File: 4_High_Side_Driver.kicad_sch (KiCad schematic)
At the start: 32 parts, among them U4 VND7050AJTR, U8 VND7050AJTR

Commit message: All the diodes, and other layout work
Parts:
- D10, D11, D12, D13, D14, D15, D16, D17, D18, D19, D20, D7, D8, D9: footprint Package_TO_SOT_SMD:SOT-23 -> Package_TO_SOT_SMD:SOT-523; LCSC C47546 -> C134414; MPN BAT54S,215 -> BAT54ST-7-F; Manufacturer Nexperia -> Diodes Incorporated
- D6: footprint Diode_SMD:D_0805_2012Metric -> Diode_SMD:D_SOD-123; LCSC (none) -> C83152; MPN (none) -> BAT46W-7-F; Manufacturer (none) -> Diodes Incorporated

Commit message: Layout, smaller resistors and HB + Error LEDs
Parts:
- D10, D11, D12, D13, D14, D17, D18, D19, D20: now in the parts list
- D6: footprint Diode_SMD:D_SOD-123 -> Diode_SMD:D_SOD-523; LCSC C83152 -> C139439; MPN BAT46W-7-F -> SDM20U40-7
- R14, R21: footprint Resistor_SMD:R_0603_1608Metric -> Resistor_SMD:R_0402_1005Metric; now in the parts list
- R15, R16, R22, R23: footprint Resistor_SMD:R_0603_1608Metric -> Resistor_SMD:R_0402_1005Metric; LCSC (none) -> C25756
- R17, R18, R19, R20, R24, R25, R26, R27: footprint Resistor_SMD:R_0603_1608Metric -> Resistor_SMD:R_0402_1005Metric; LCSC (none) -> C25756; now in the parts list
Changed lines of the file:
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@@
 		(unit 1)
 		(exclude_from_sim no)
-		(in_bom no)
-		(on_board no)
+		(in_bom yes)
+		(on_board yes)
 		(dnp no)
 		(fields_autoplaced yes)
@@
 		(unit 1)
 		(exclude_from_sim no)
-		(in_bom no)
-		(on_board no)
+		(in_bom yes)
+		(on_board yes)
 		(dnp no)
 		(property "Reference" "R26"
@@
 			)
 		)
-		(property "Footprint" "Resistor_SMD:R_0603_1608Metric"
+		(property "Footprint" "Resistor_SMD:R_0402_1005Metric"
 			(at 139.7 102.362 90)
 			(effects
@@
 			)
 		)
-		(property "LCSC" ""
+		(property "LCSC" "C25756"
 			(at 139.7 104.14 0)
 			(effects
@@
 		(unit 1)
 		(exclude_from_sim no)
-		(in_bom no)
-		(on_board no)
+		(in_bom yes)
+		(on_board yes)
 		(dnp no)
 		(fields_autoplaced yes)
@@
 		(unit 1)
 		(exclude_from_sim no)
-		(in_bom no)
-		(on_board no)
+		(in_bom yes)
+		(on_board yes)
 		(dnp no)
 		(property "Reference" "R27"
@@
 			)
 		)
-		(property "Footprint" "Resistor_SMD:R_0603_1608Metric"
+		(property "Footprint" "Resistor_SMD:R_0402_1005Metric"
 			(at 139.7 104.902 90)
 			(effects
@@
 			)
 		)
-		(property "LCSC" ""
+		(property "LCSC" "C25756"
 			(at 139.7 106.68 0)
 			(effects
@@
 			)
 		)
-		(property "Footprint" "Resistor_SMD:R_0603_1608Metric"
+		(property "Footprint" "Resistor_SMD:R_0402_1005Metric"
 			(at 139.7 92.202 90)
 			(effects
@@
 			)
 		)
-		(property "LCSC" ""
+		(property "LCSC" "C25756"
 			(at 139.7 93.98 0)
 			(effects
@@
 		(unit 1)
 		(exclude_from_sim no)
-		(in_bom no)
-		(on_board no)
+		(in_bom yes)
+		(on_board yes)
 		(dnp no)
 		(fields_autoplaced yes)
@@
 			)
 		)
-		(property "Footprint" "Resistor_SMD:R_0603_1608Metric"
+		(property "Footprint" "Resistor_SMD:R_0402_1005Metric"
 			(at 139.7 89.662 90)
 			(effects
@@
 			)
 		)
-		(property "LCSC" ""
+		(property "LCSC" "C25756"
 			(at 139.7 91.44 0)
 			(effects
@@
 		(unit 1)
 		(exclude_from_sim no)
-		(in_bom no)
-		(on_board no)
+		(in_bom yes)
+		(on_board yes)
 		(dnp no)
 		(property "Reference" "R17"
@@
 			)
 		)
-		(property "Footprint" "Resistor_SMD:R_0603_1608Metric"
+		(property "Footprint" "Resistor_SMD:R_0402_1005Metric"
 			(at 50.8 97.282 90)
 			(effects
@@
 			)
 		)
-		(property "LCSC" ""
+		(property "LCSC" "C25756"
 			(at 50.8 99.06 0)
 			(effects
@@
 			)
 		)
-		(property "Footprint" "Diode_SMD:D_SOD-123"
+		(property "Footprint" "Diode_SMD:D_SOD-523"
 			(at 114.3 161.29 0)
 			(effects
@@
 			)
 		)
-		(property "Datasheet" "https://www.lcsc.com/datasheet/lcsc_datasheet_2412251151_Diodes-Incorporated-BAT46W-7-F_C83152.pdf"
+		(property "Datasheet" "https://www.lcsc.com/datasheet/lcsc_datasheet_2412251002_Diodes-Incorporated-SDM20U40-7_C139439.pdf"
 			(at 114.3 161.29 0)
 			(effects
@@
 			)
 		)
-		(property "LCSC" "C83152"
+		(property "LCSC" "C139439"
 			(at 114.3 161.29 0)
 			(effects
@@
 			)
 		)
-		(property "MPN" "BAT46W-7-F"
+		(property "MPN" "SDM20U40-7"
 			(at 114.3 161.29 0)
 			(effects
@@
 		(unit 1)
 		(exclude_from_sim no)
-		(in_bom no)
-		(on_board no)
+		(in_bom yes)
+		(on_board yes)
 		(dnp no)
 		(property "Reference" "R21"
@@
 			)
 		)
-		(property "Footprint" "Resistor_SMD:R_0603_1608Metric"
+		(property "Footprint" "Resistor_SMD:R_0402_1005Metric"
 			(at 139.7 84.582 90)
 			(effects
@@
 		(unit 1)
 		(exclude_from_sim no)
-		(in_bom no)
-		(on_board no)
+		(in_bom yes)
+		(on_board yes)
 		(dnp no)
 		(fields_autoplaced yes)
@@
 			)
 		)
-		(property "Footprint" "Resistor_SMD:R_0603_1608Metric"
+		(property "Footprint" "Resistor_SMD:R_0402_1005Metric"
 			(at 50.8 92.202 90)
 			(effects
@@
 			)
 		)
-		(property "LCSC" ""
+		(property "LCSC" "C25756"
 			(at 50.8 93.98 0)
 			(effects
@@
 		(unit 1)
 		(exclude_from_sim no)
-		(in_bom no)
-		(on_board no)
+		(in_bom yes)
+		(on_board yes)
 		(dnp no)
 		(fields_autoplaced yes)
@@
 		(unit 1)
 		(exclude_from_sim no)
-		(in_bom no)
-		(on_board no)
+		(in_bom yes)
+		(on_board yes)
 		(dnp no)
 		(property "Reference" "R20"
@@
 			)
 		)
-		(property "Footprint" "Resistor_SMD:R_0603_1608Metric"
+		(property "Footprint" "Resistor_SMD:R_0402_1005Metric"
 			(at 50.8 104.902 90)
 			(effects
@@
 			)
 		)
-		(property "LCSC" ""
+		(property "LCSC" "C25756"
 			(at 50.8 106.68 0)
 			(effects
@@
 		(unit 1)
 		(exclude_from_sim no)
-		(in_bom no)
-		(on_board no)
+		(in_bom yes)
+		(on_board yes)
 		(dnp no)
 		(property "Reference" "R19"
@@
 			)
 		)
-		(property "Footprint" "Resistor_SMD:R_0603_1608Metric"
+		(property "Footprint" "Resistor_SMD:R_0402_1005Metric"
 			(at 50.8 102.362 90)
 			(effects
@@
 			)
 		)
-		(property "LCSC" ""
+		(property "LCSC" "C25756"
 			(at 50.8 104.14 0)
 			(effects
@@
 			)
 		)
-		(property "Footprint" "Resistor_SMD:R_0603_1608Metric"
+		(property "Footprint" "Resistor_SMD:R_0402_1005Metric"
 			(at 50.8 89.662 90)
 			(effects
@@
 			)
 		)
-		(property "LCSC" ""
+		(property "LCSC" "C25756"
 			(at 50.8 91.44 0)
 			(effects
@@
 		(unit 1)
 		(exclude_from_sim no)
-		(in_bom no)
-		(on_board no)
+		(in_bom yes)
+		(on_board yes)
 		(dnp no)
 		(property "Reference" "R18"
@@
 			)
 		)
-		(property "Footprint" "Resistor_SMD:R_0603_1608Metric"
+		(property "Footprint" "Resistor_SMD:R_0402_1005Metric"
 			(at 50.8 99.822 90)
 			(effects
@@
 			)
 		)
-		(property "LCSC" ""
+		(property "LCSC" "C25756"
 			(at 50.8 101.6 0)
 			(effects
@@
 		(unit 1)
 		(exclude_from_sim no)
-		(in_bom no)
-		(on_board no)
+		(in_bom yes)
+		(on_board yes)
 		(dnp no)
 		(fields_autoplaced yes)
@@
 		(unit 1)
 		(exclude_from_sim no)
-		(in_bom no)
-		(on_board no)
+		(in_bom yes)
+		(on_board yes)
 		(dnp no)
 		(property "Reference" "R24"
@@
 			)
 		)
-		(property "Footprint" "Resistor_SMD:R_0603_1608Metric"
+		(property "Footprint" "Resistor_SMD:R_0402_1005Metric"
 			(at 139.7 97.282 90)
 			(effects
@@
 			)
 		)
-		(property "LCSC" ""
+		(property "LCSC" "C25756"
 			(at 139.7 99.06 0)
 			(effects
@@
 		(unit 1)
 		(exclude_from_sim no)
-		(in_bom no)
-		(on_board no)
+		(in_bom yes)
+		(on_board yes)
 		(dnp no)
 		(fields_autoplaced yes)
@@
 		(unit 1)
 		(exclude_from_sim no)
-		(in_bom no)
-		(on_board no)
+		(in_bom yes)
+		(on_board yes)
 		(dnp no)
 		(property "Reference" "R25"
@@
 			)
 		)
-		(property "Footprint" "Resistor_SMD:R_0603_1608Metric"
+		(property "Footprint" "Resistor_SMD:R_0402_1005Metric"
 			(at 139.7 99.822 90)
 			(effects
@@
 			)
 		)
-		(property "LCSC" ""
+		(property "LCSC" "C25756"
 			(at 139.7 101.6 0)
 			(effects
@@
 		(unit 1)
 		(exclude_from_sim no)
-		(in_bom no)
-		(on_board no)
+		(in_bom yes)
+		(on_board yes)
 		(dnp no)
 		(property "Reference" "R14"
@@
 			)
 		)
-		(property "Footprint" "Resistor_SMD:R_0603_1608Metric"
+		(property "Footprint" "Resistor_SMD:R_0402_1005Metric"
 			(at 50.8 84.582 90)
 			(effects
@@
 		(unit 1)
 		(exclude_from_sim no)
-		(in_bom no)
-		(on_board no)
+		(in_bom yes)
+		(on_board yes)
 		(dnp no)
 		(fields_autoplaced yes)
@@
 		(unit 1)
 		(exclude_from_sim no)
-		(in_bom no)
-		(on_board no)
+		(in_bom yes)
+		(on_board yes)
 		(dnp no)
 		(fields_autoplaced yes)

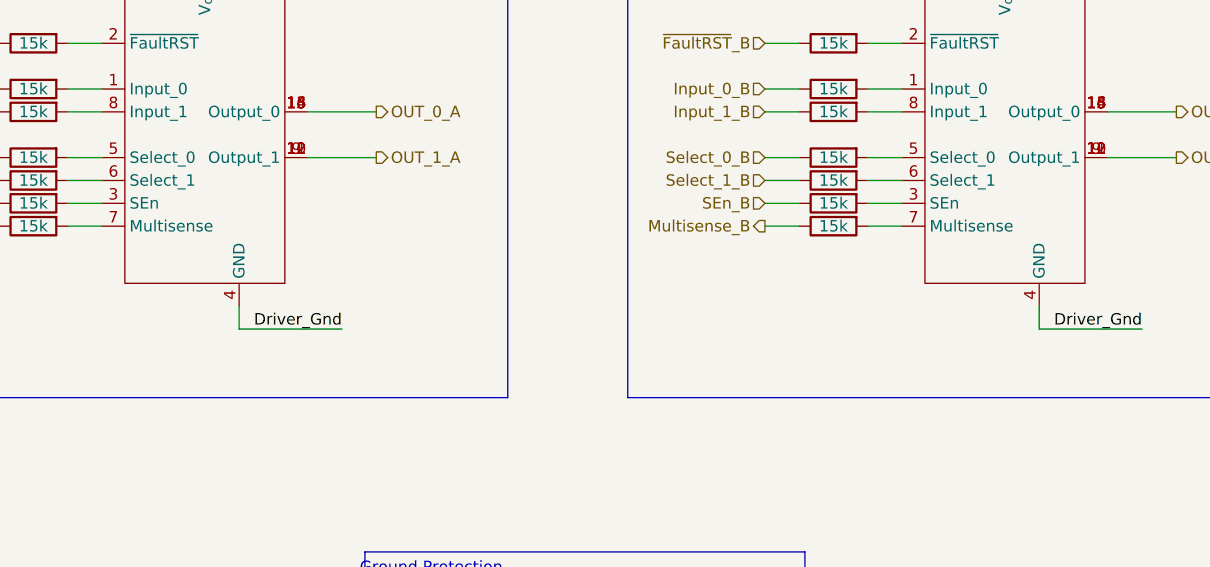
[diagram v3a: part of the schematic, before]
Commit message: Finalised RS485 Circuit, Layout improvemnts, mounting holes, silkscreen...
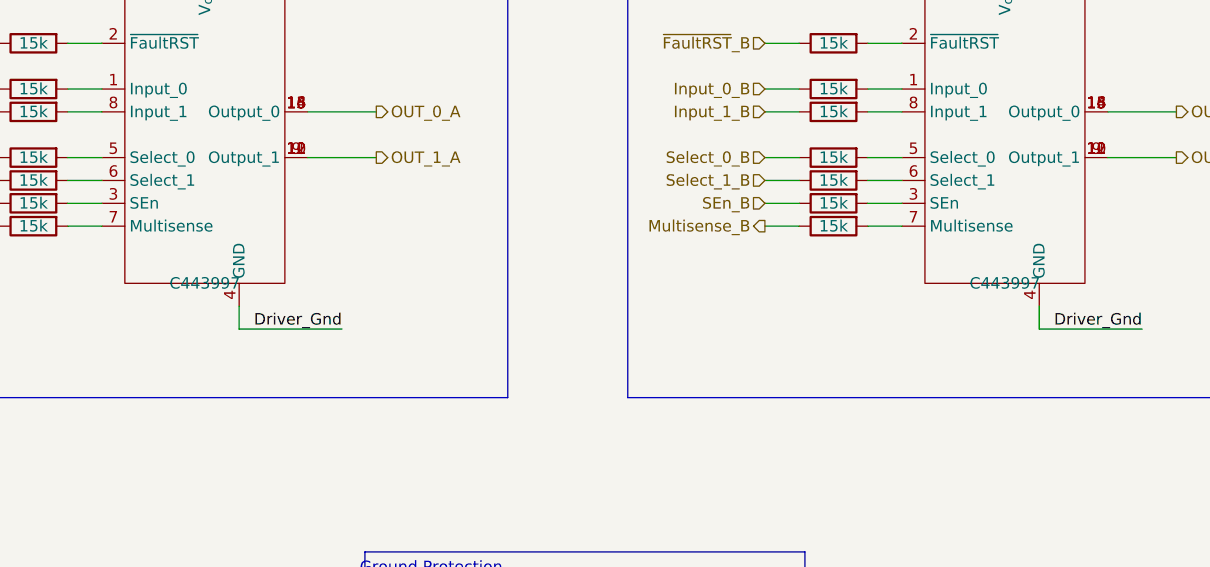
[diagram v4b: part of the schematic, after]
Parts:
- R14, R21: LCSC (none) -> C25756
- U4, U8: LCSC (none) -> C443997
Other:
- company: (none) -> eChook
- title: (none) -> BMS Comms Master Board
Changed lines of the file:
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@@
 	(generator_version "9.0")
 	(paper "A4")
+	(title_block
+		(title "BMS Comms Master Board")
+		(date "2025-05-21")
+		(rev "0.1")
+		(company "eChook")
+	)
 	(rectangle
 		(start 116.84 62.23)
@@
 			)
 		)
-		(property "LCSC" ""
+		(property "LCSC" "C25756"
 			(at 139.7 86.36 0)
 			(effects
@@
 			)
 		)
+		(property "LCSC" "C443997"
+			(at 158.75 113.03 0)
+			(effects
+				(font
+					(size 1.27 1.27)
+				)
+			)
+		)
 		(pin "9"
 		)
@@
 			)
 		)
+		(property "LCSC" "C443997"
+			(at 69.85 113.03 0)
+			(effects
+				(font
+					(size 1.27 1.27)
+				)
+			)
+		)
 		(pin "9"
 		)
@@
 			)
 		)
-		(property "LCSC" ""
+		(property "LCSC" "C25756"
 			(at 50.8 86.36 0)
 			(effects

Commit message: Schematic Net Colours
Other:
- note added: "TODO - Add Sense Resistor"
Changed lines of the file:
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@@
+		)
+	)
+	(text "TODO - Add Sense Resistor"
+		(exclude_from_sim no)
+		(at 108.204 133.604 0)
+		(effects
+			(font
+				(size 1.27 1.27)
+			)
 		)
 	)

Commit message: PCB Improvements - VIAS/Pours UNFINISHED
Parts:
- added C29, C30: 10uF, Capacitor_SMD:C_0805_2012Metric, symbol Device:C
- added C31, C32: 0.1uF, Capacitor_SMD:C_0402_1005Metric, symbol Device:C
- added R81, R82: 680, Resistor_SMD:R_0603_1608Metric, symbol Device:R
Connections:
- net GND: now also C29.1, C30.1, C31.1, C32.1, R81.1, R82.1
- net Multisense_A: now also C32.2
- net Multisense_B: now also C31.2
- net V_{CC}: now also C29.2, C30.2
- net at R27.2, U8.7 (Multisense): now also R81.2
- net at R20.2, U4.7 (Multisense): now also R82.2

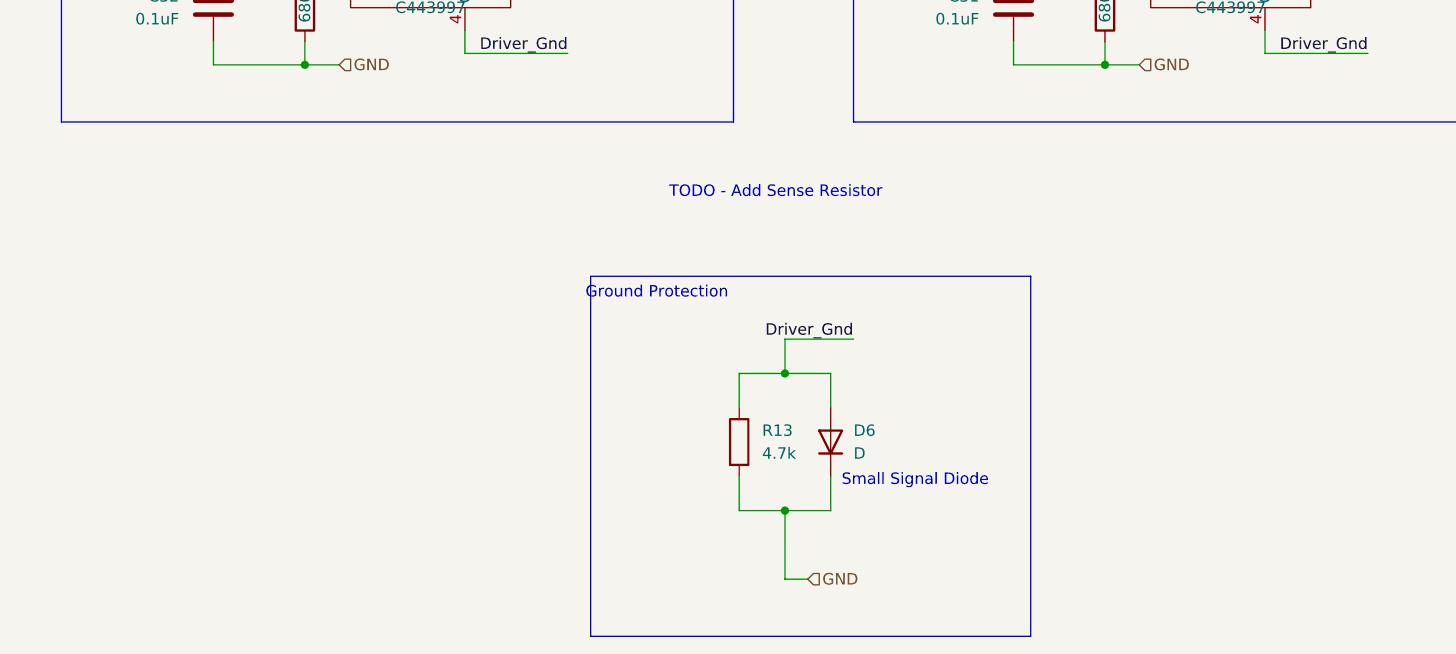
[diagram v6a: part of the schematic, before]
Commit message: Added pulldown safety resistors, layout improvements
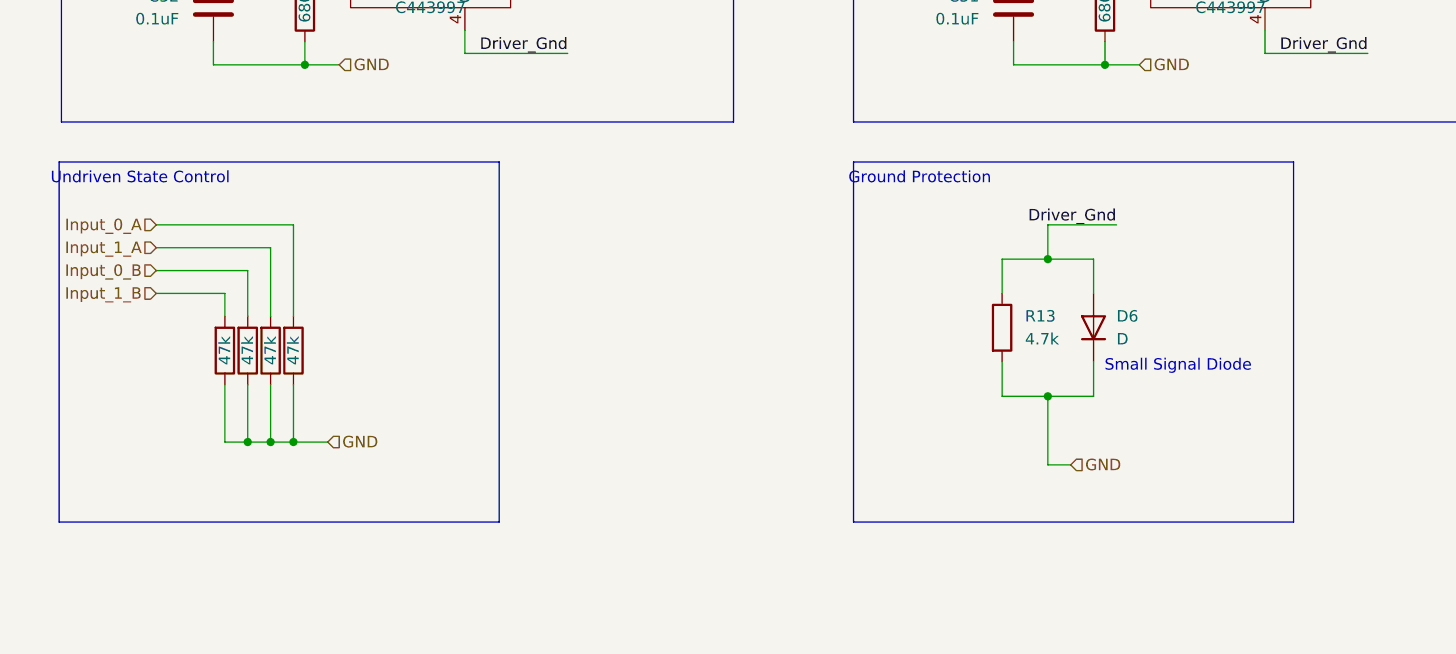
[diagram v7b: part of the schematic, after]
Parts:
- added R83, R84, R85, R86: 47k, Resistor_SMD:R_0603_1608Metric, symbol Device:R
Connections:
- net GND: now also R83.1, R84.1, R85.1, R86.1
- net Input_0_A: now also R86.2
- net Input_0_B: now also R84.2
- net Input_1_A: now also R85.2
- net Input_1_B: now also R83.2
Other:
- note added: "Undriven State Control"
- note removed: "TODO - Add Sense Resistor"
- moved on the sheet: D6, R13
